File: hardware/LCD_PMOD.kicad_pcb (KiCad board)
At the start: 2 copper layers, 175.3 x 95.2 mm, 169 parts, among them IC1 TPS61169DCKR, IC2 TPD4E001DRLR, IC3 AR1021-I/SS, IC4 M24C32-WMN6P, J1 20-pin power socket, J10 OS0, J11 OS1, J12 OS2, J13 PAR, J14 RANGE, J15 REF, J16 MDD01, J17 FTDI, J18 Conn_01x10, J2 VS_SCL, J3 28-pin module socket, J4 691327310016, J5 691327310016, J6 HS_SDA, J7 JMP_A0, J8 DE_IRQ, J9 DIB_V2, U1 ADS8586S, U2 REF5025AD, U3 DS90CF364AMTD, U4 DS90CF36B, U5 MC78L05_SO8, U6 THS4032ID, U7 THS4551IDGKT, U8 THS4551IDGKT, U9 MC79L05_SO8

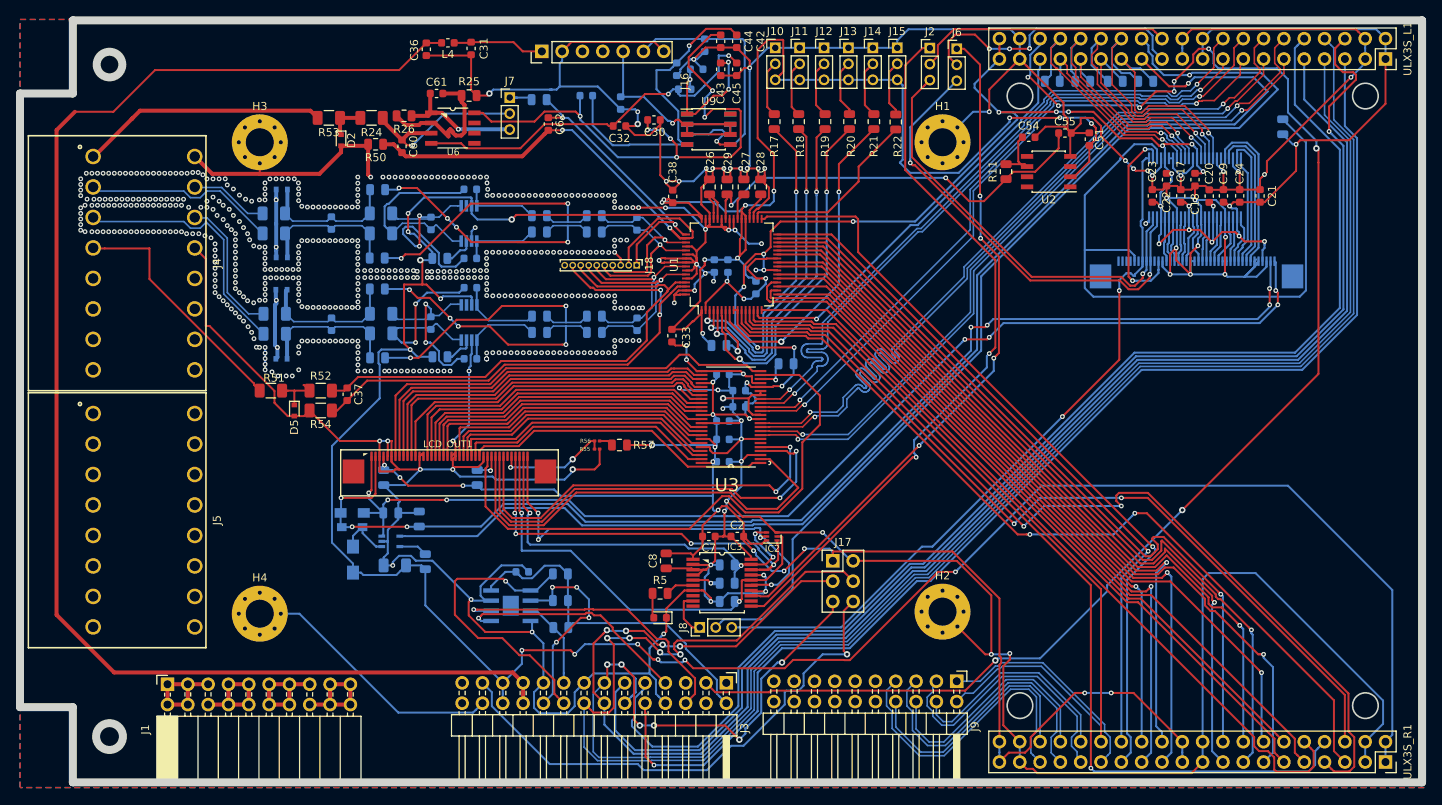
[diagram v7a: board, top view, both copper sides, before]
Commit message: Rerouting
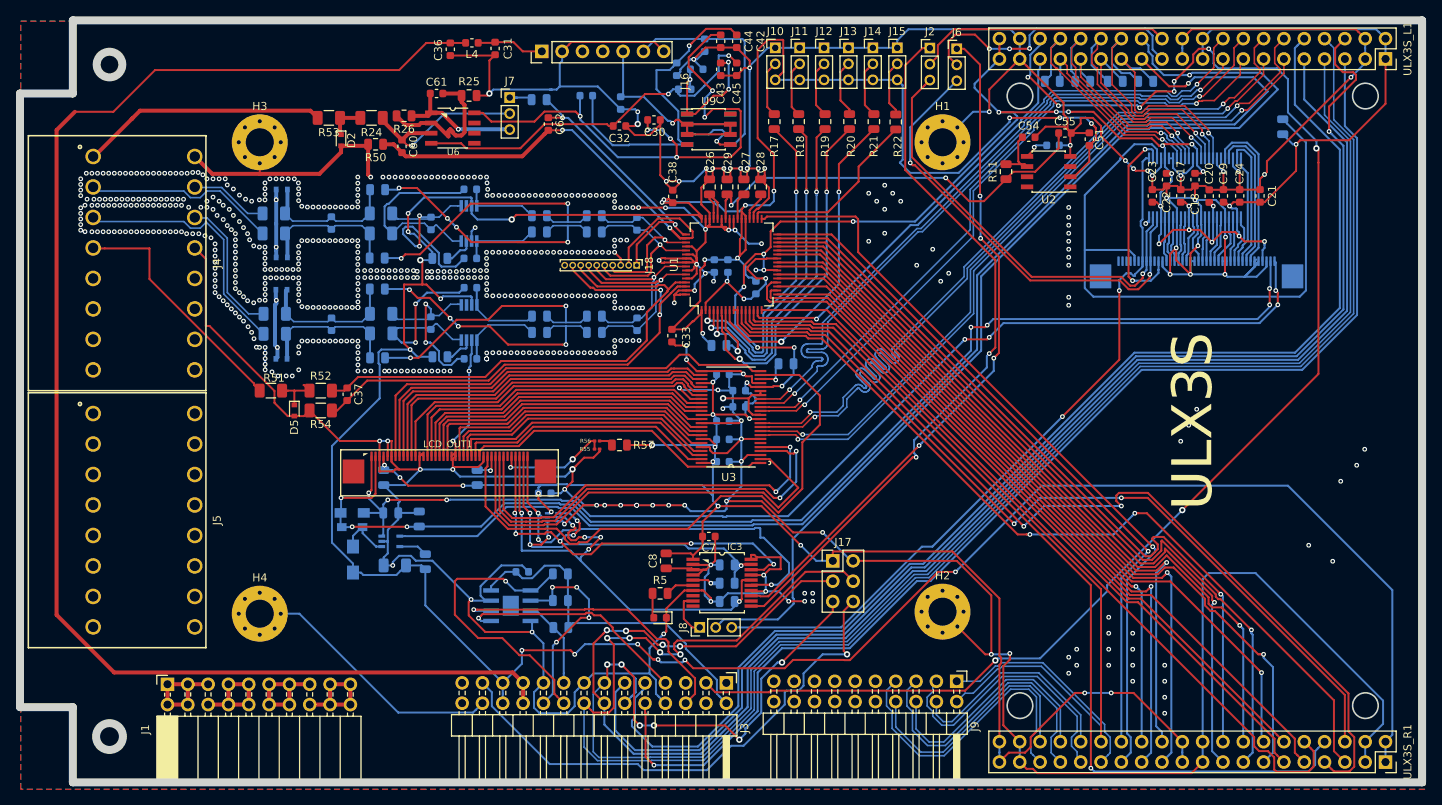
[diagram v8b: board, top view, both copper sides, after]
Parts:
- added C46: 1u, Capacitor_SMD:C_0603_1608Metric, B.Cu at (187.0, 56.0)
- C2, IC2: moved to B.Cu
- C51: value 1uF -> 4.7uF
- moved IC2 27.5 mm to (124.5, 102.5)
- moved C2 24.7 mm to (123.5, 99.5), turned to 180 degrees
- moved C31 3.00 mm to (117.3, 43.9)
- moved C36 3.00 mm to (111.7, 44.0)
- moved L4 3.00 mm to (114.4, 43.2)
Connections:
- U2 pad 5: (no net) -> Net-(C46-Pad1)
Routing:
- net GND: track 1053.8 -> 1090.0 mm, vias 554 -> 615
- net /LCD/Touch_YD: track 55.9 -> 59.9 mm, vias 2 -> 6
- net /LCD/Touch_XL: track 52.3 -> 48.6 mm
- net Net-(C46-Pad1): track 0.00 -> 3.17 mm, vias 0 -> 1
- net +12V: track 177.6 -> 180.6 mm
- net Net-(C31-Pad1): track 11.5 -> 8.47 mm
- net /LCD/Touch_XR: track 52.1 -> 55.1 mm, vias 4 -> 7
- net LTDC_CLK: track 71.9 -> 73.7 mm
- net 8P: track 128.1 -> 129.4 mm
- net 3V3: track 439.2 -> 438.2 mm
- net /LCD/Touch_YU: track 52.9 -> 53.7 mm, vias 4 -> 3
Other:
- board text added: "ULX3S"
